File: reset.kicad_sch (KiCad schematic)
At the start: 21 parts, among them J4 MAINCLK, K15 74LS04

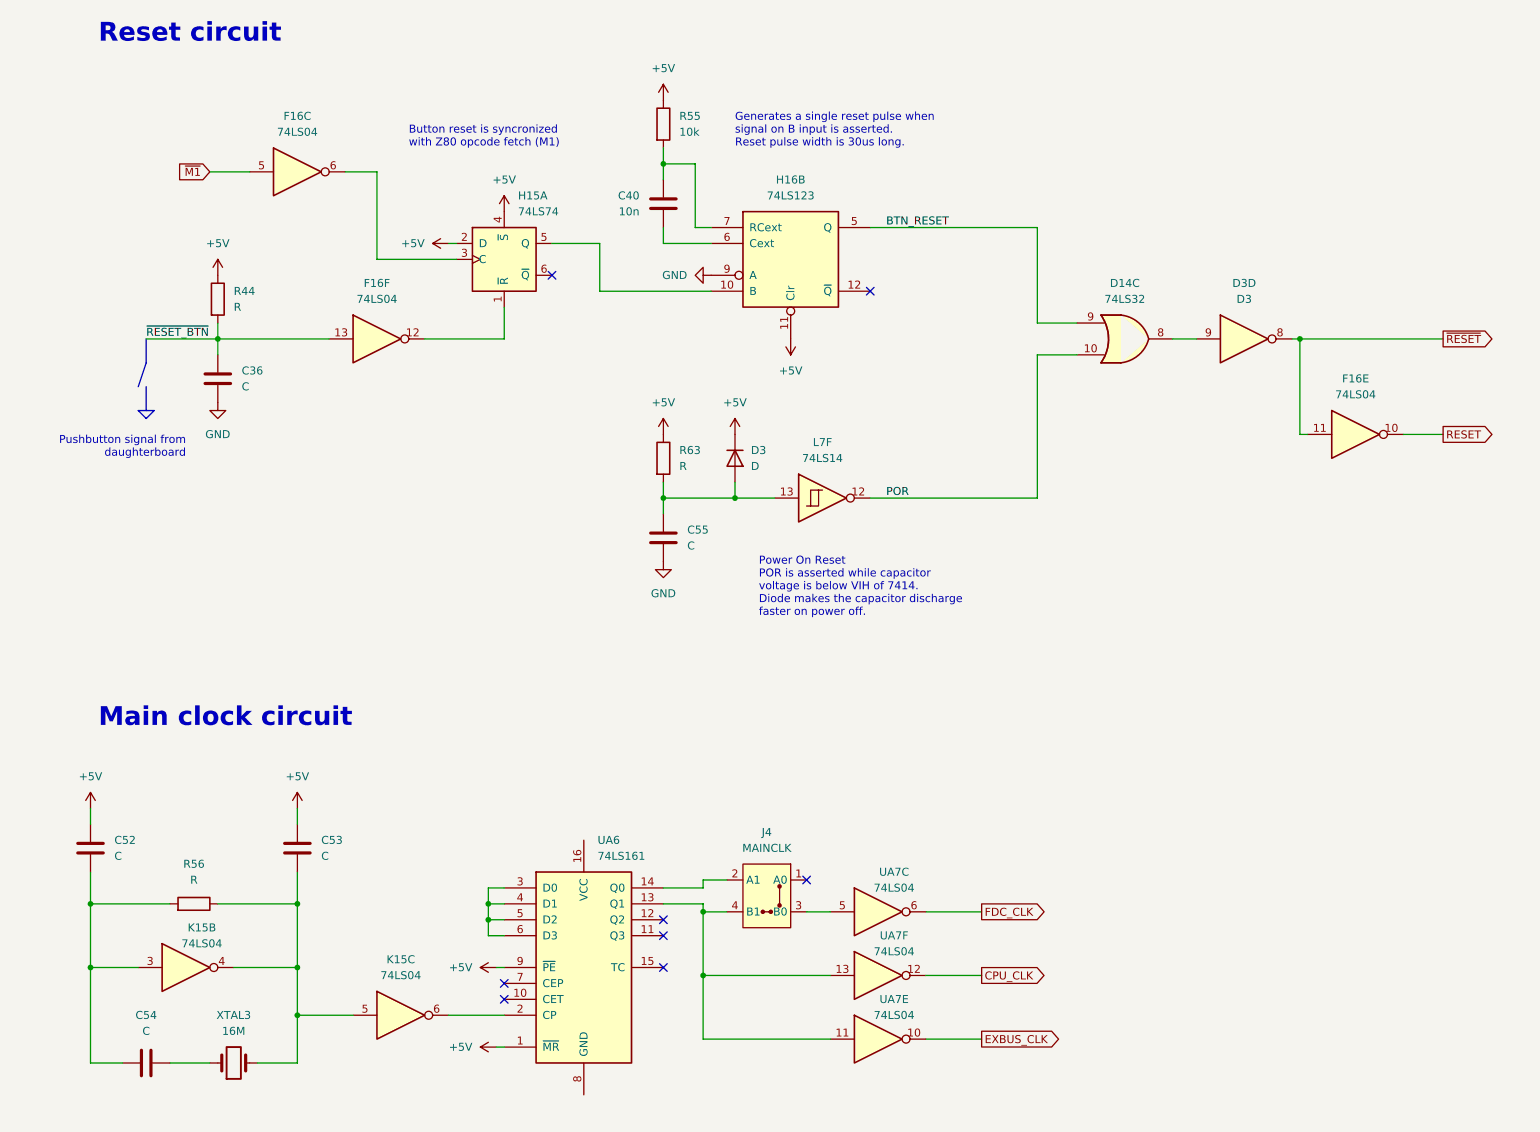
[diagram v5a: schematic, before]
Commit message: Components renaming according to the Uxy convention.
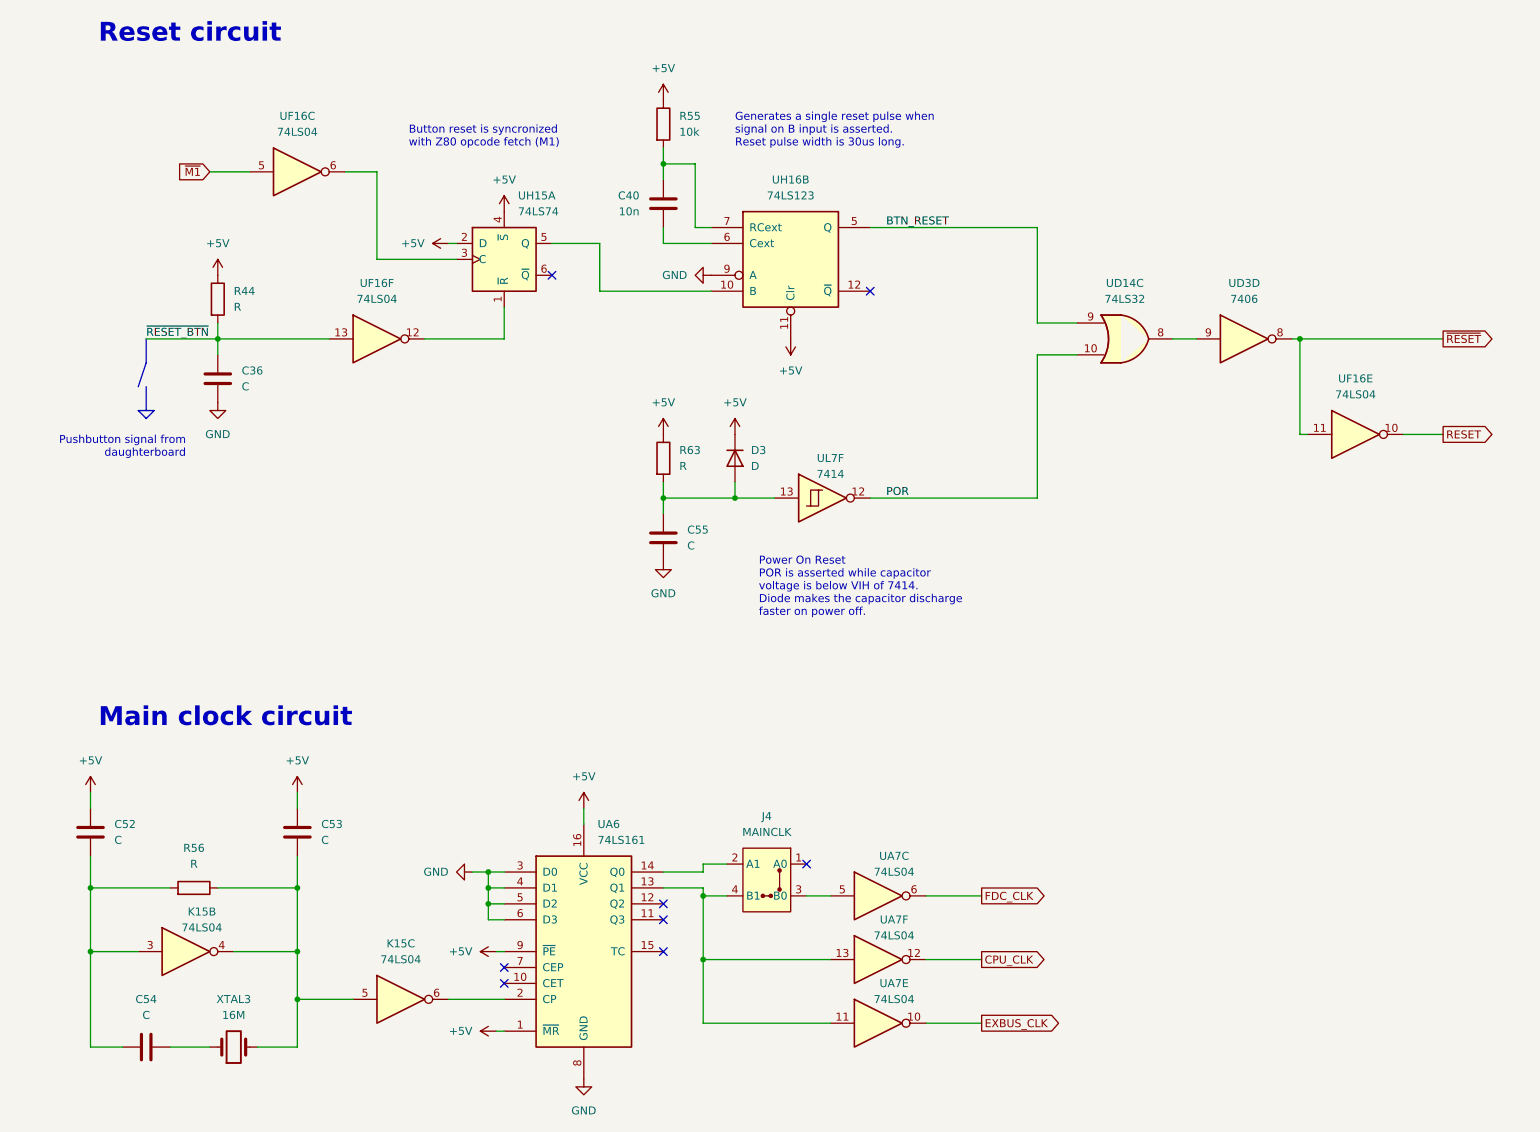
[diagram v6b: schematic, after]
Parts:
- UD3: renamed from D3; value D3 -> 7406
- UL7: renamed from L7; value 74LS14 -> 7414
- renumbered D14 to UD14, F16 to UF16, H15 to UH15, H16 to UH16
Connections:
- net +5V: now also UA6.16 (VCC)
- net GND: now also UA6.3 (D0), UA6.4 (D1), UA6.5 (D2), UA6.6 (D3), UA6.8 (GND)
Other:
- moved on the sheet: C52, C53, C54, J4, K15B, K15C, R56, UA6, UA7C, UA7E, UA7F, XTAL3

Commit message: Notes in kicad's sheet text blocks
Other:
- company: (none) -> Logic Systems Int'l Inc
- title: (none) -> CEDA - Sanco 8003 schematics
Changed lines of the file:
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@@
   (paper "A4")
   (title_block
-    (comment 1 "Reset and main clock")
+    (title "CEDA - Sanco 8003 schematics")
+    (rev "05")
+    (company "Logic Systems Int'l Inc")
+    (comment 1 "reversed by RetrOfficina - retrofficina.glgprograms.it")
+    (comment 4 "Main clock and reset")
   )
   (junction (at 40.64 72.39) (diameter 0) (color 0 0 0 0)

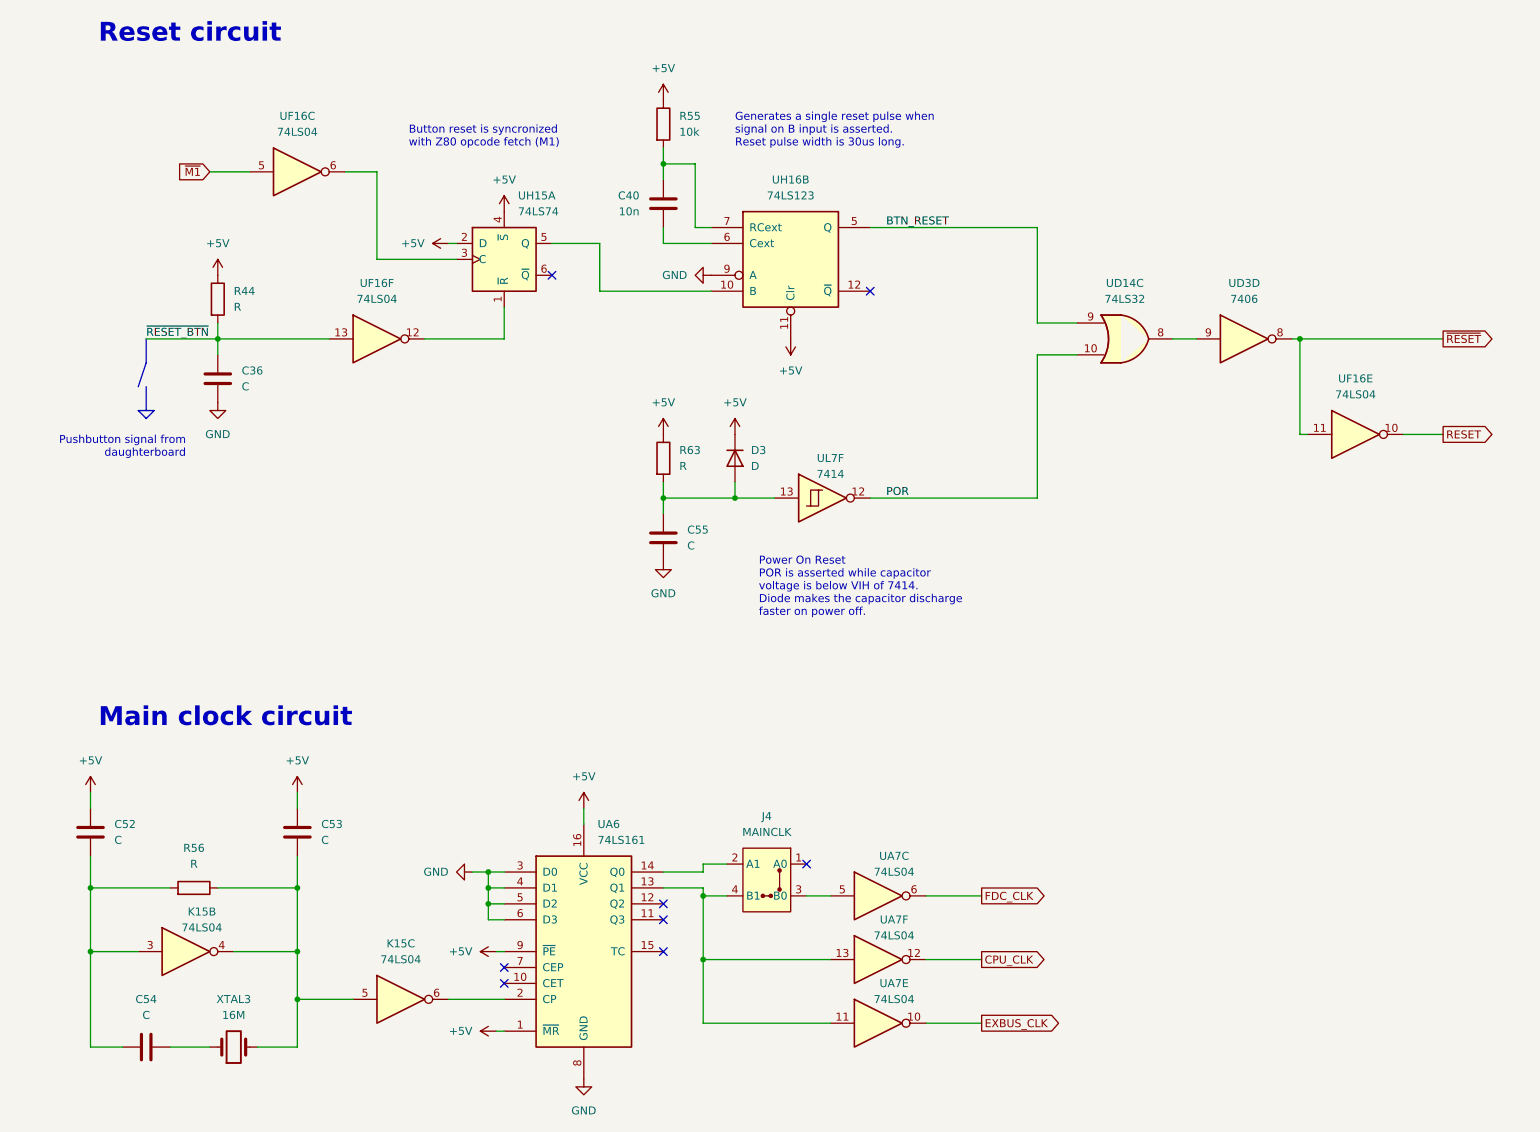
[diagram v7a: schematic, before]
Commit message: Upgrade to KiCAD 9.0
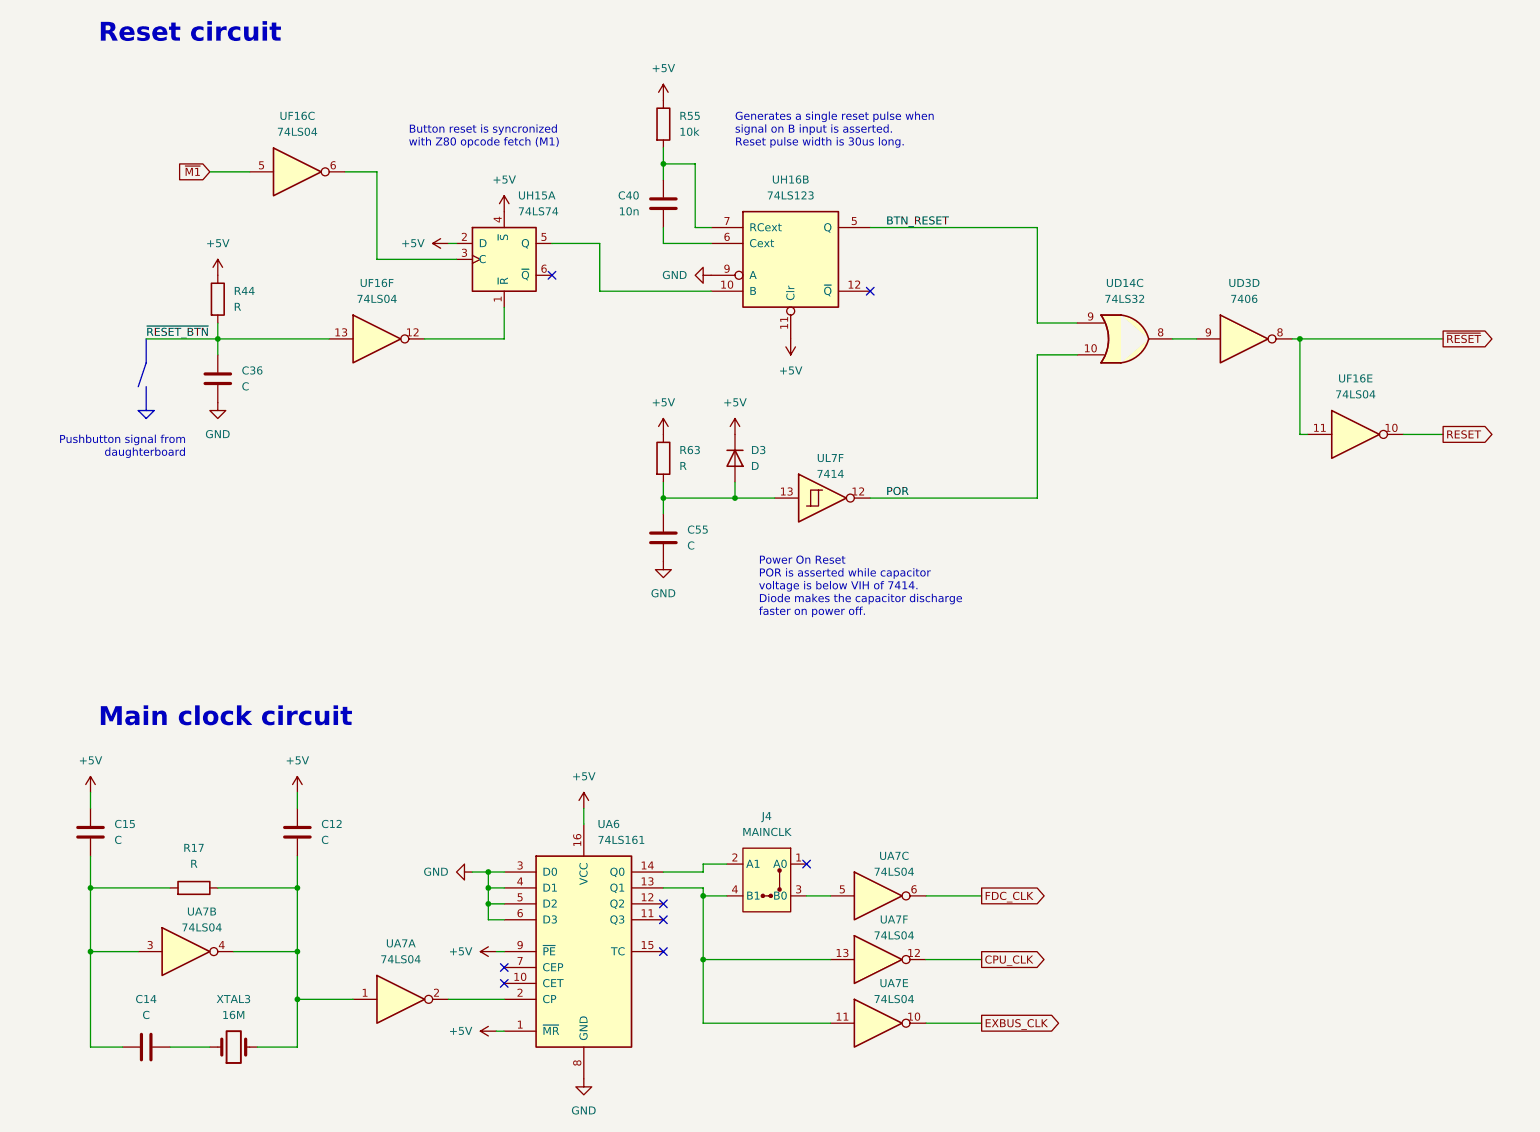
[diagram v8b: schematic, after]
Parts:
- renumbered C53 to C12, C54 to C14, C52 to C15, R56 to R17, K15 to UA7
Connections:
- net at UA6.2 (CP): now also UA7.2; no longer UA7.6
- net at C12.1, R17.1, UA7.4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: now also UA7.1; no longer UA7.5
